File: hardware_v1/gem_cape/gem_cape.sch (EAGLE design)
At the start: 16 parts, among them P8 TSW-123-05-G-D, P9 TSW-123-05-G-D, U1 SN65HVD379, U2 SN65HVD379

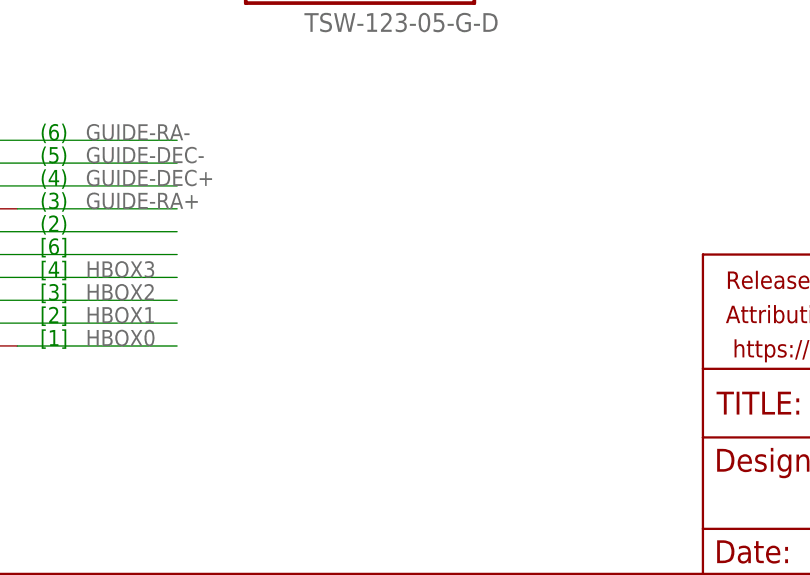
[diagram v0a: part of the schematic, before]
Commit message: hardware_v1/gem_cape: add hpad truth to schematic
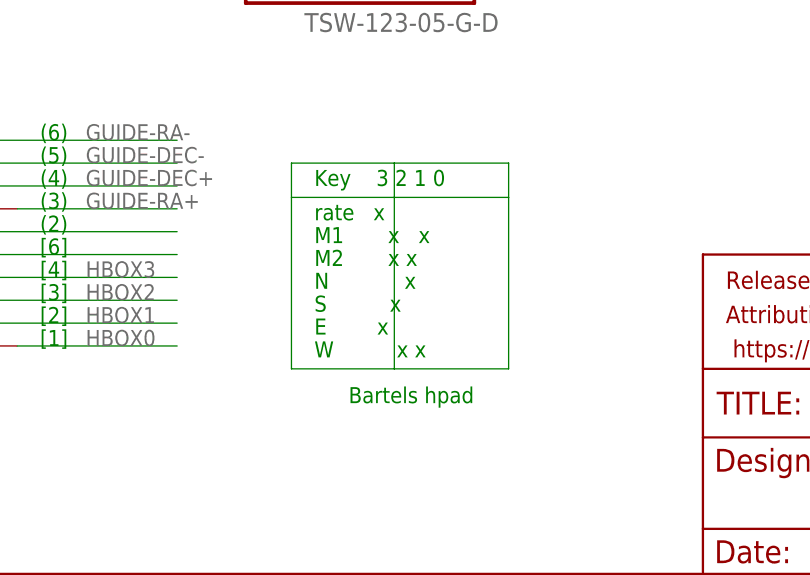
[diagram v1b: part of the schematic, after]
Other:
- note added: "Bartels hpad"
- note added: "E x"
- note added: "Key 3 2 1 0"
- note added: "M1 x x"
- note added: "M2 x x"
- note added: "N x"
- note added: "S x"
- note added: "W x x"
- note added: "rate x"
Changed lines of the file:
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@@
 <setting verticaltext="up"/>
 </settings>
-<grid distance="0.1" unitdist="inch" unit="inch" style="lines" multiple="1" display="no" altdistance="0.01" altunitdist="inch" altunit="inch"/>
+<grid distance="0.05" unitdist="inch" unit="inch" style="lines" multiple="1" display="no" altdistance="0.01" altunitdist="inch" altunit="inch"/>
 <layers>
 <layer number="1" name="Top" color="4" fill="1" visible="no" active="no"/>
@@
 <text x="109.22" y="71.12" size="1.778" layer="91">gpio73</text>
 <text x="101.6" y="68.58" size="1.778" layer="91">gpio70</text>
+<text x="104.14" y="39.37" size="1.778" layer="91" font="fixed">rate   x</text>
+<text x="104.14" y="36.83" size="1.778" layer="91" font="fixed">M1       x   x</text>
+<text x="104.14" y="34.29" size="1.778" layer="91" font="fixed">M2       x x </text>
+<text x="104.14" y="43.18" size="1.778" layer="91" font="fixed">Key    3 2 1 0</text>
+<text x="104.14" y="31.75" size="1.778" layer="91" font="fixed">N            x</text>
+<text x="104.14" y="29.21" size="1.778" layer="91" font="fixed">S          x</text>
+<text x="104.14" y="26.67" size="1.778" layer="91" font="fixed">E        x</text>
+<text x="104.14" y="24.13" size="1.778" layer="91" font="fixed">W          x x</text>
+<text x="107.95" y="19.05" size="1.778" layer="91">Bartels hpad</text>
 </plain>
 <instances>
@@
 </segment>
 </net>
+<net name="N$1" class="0">
+<segment>
+<wire x1="101.6" y1="45.72" x2="113.03" y2="45.72" width="0.1524" layer="91"/>
+<wire x1="113.03" y1="45.72" x2="125.73" y2="45.72" width="0.1524" layer="91"/>
+<wire x1="125.73" y1="45.72" x2="125.73" y2="41.91" width="0.1524" layer="91"/>
+<wire x1="125.73" y1="41.91" x2="125.73" y2="22.86" width="0.1524" layer="91"/>
+<wire x1="125.73" y1="22.86" x2="113.03" y2="22.86" width="0.1524" layer="91"/>
+<wire x1="113.03" y1="22.86" x2="101.6" y2="22.86" width="0.1524" layer="91"/>
+<wire x1="101.6" y1="22.86" x2="101.6" y2="41.91" width="0.1524" layer="91"/>
+<wire x1="101.6" y1="41.91" x2="101.6" y2="45.72" width="0.1524" layer="91"/>
+<wire x1="101.6" y1="41.91" x2="125.73" y2="41.91" width="0.1524" layer="91"/>
+<wire x1="113.03" y1="45.72" x2="113.03" y2="22.86" width="0.1524" layer="91"/>
+</segment>
+</net>

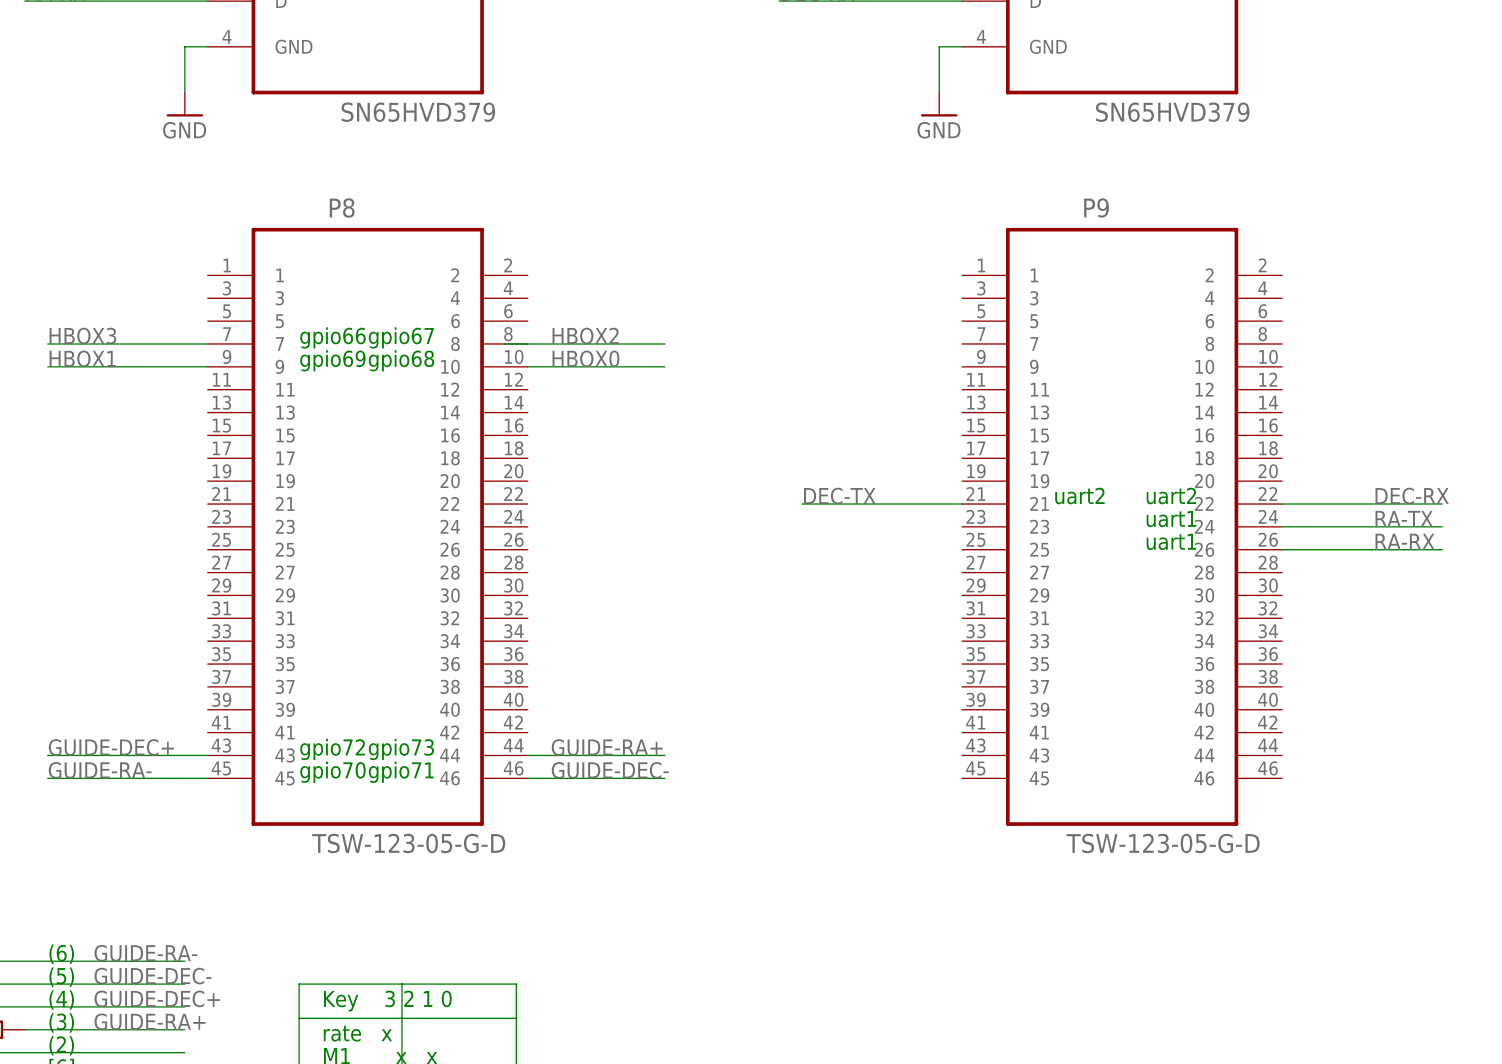
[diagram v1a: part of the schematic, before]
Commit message: hardware_v1/gem_cape: add power pins
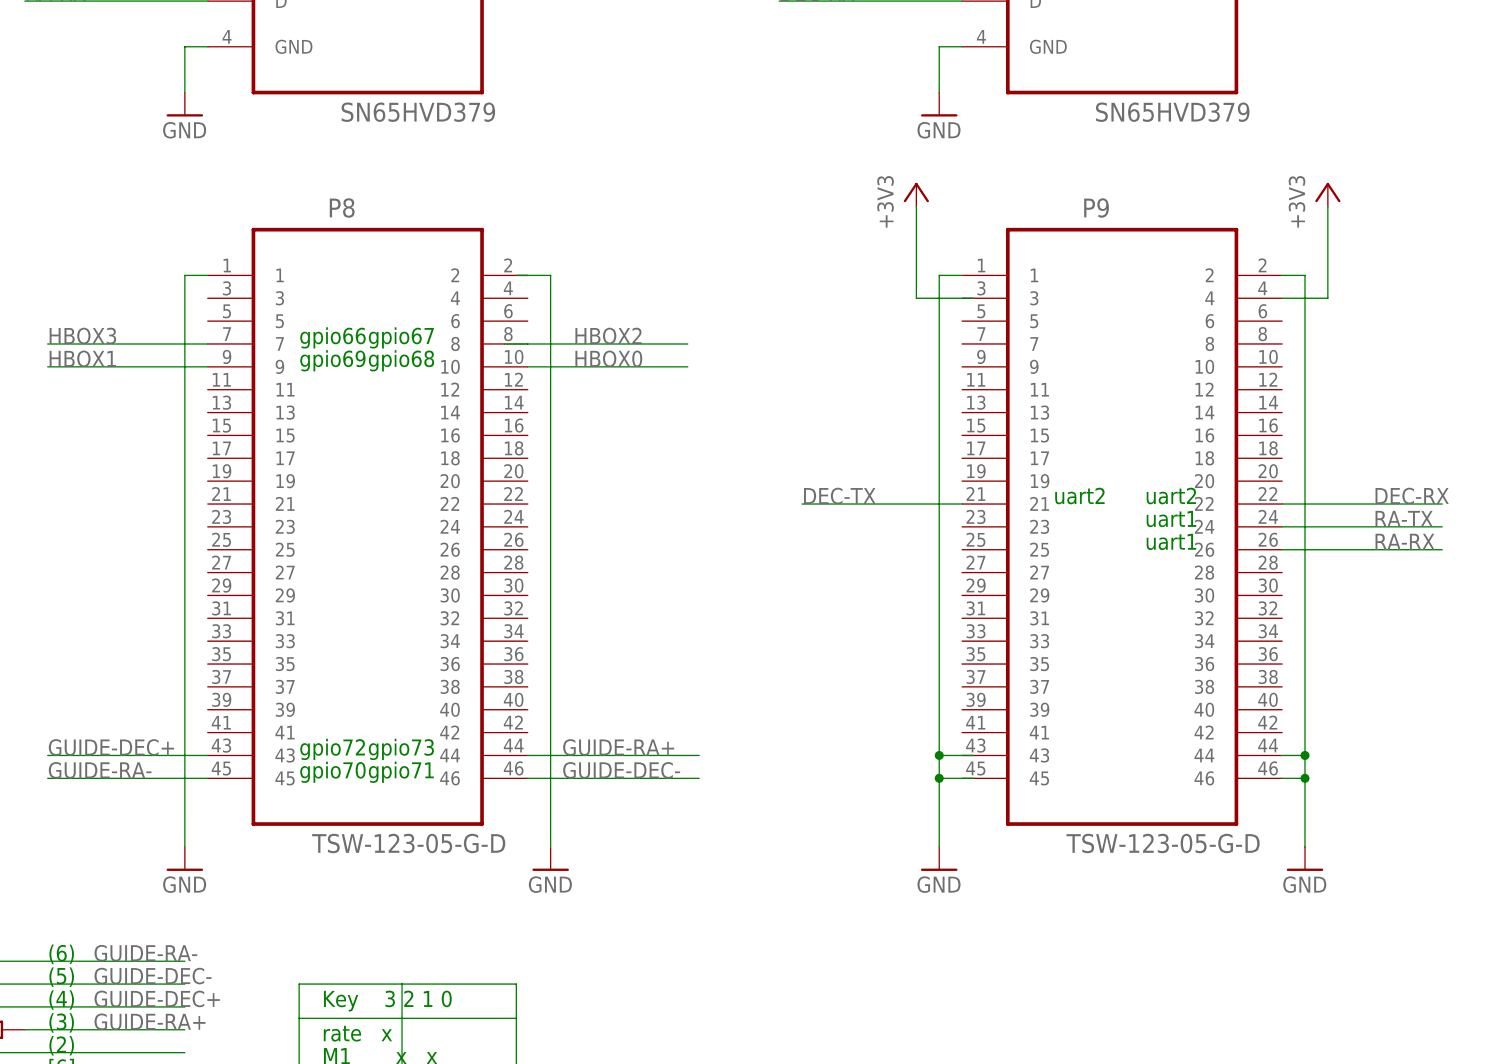
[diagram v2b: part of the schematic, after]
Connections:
- net +3V3: now also P9.4
- net GND: now also P8.1, P9.1, P9.2, P9.44, P9.46
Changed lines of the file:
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@@
 <part name="R7" library="resistor" deviceset="R-EU_" device="R0805" value="220"/>
 <part name="R8" library="resistor" deviceset="R-EU_" device="R0805" value="220"/>
+<part name="GND6" library="supply1" deviceset="GND" device=""/>
+<part name="GND7" library="supply1" deviceset="GND" device=""/>
+<part name="GND8" library="supply1" deviceset="GND" device=""/>
+<part name="GND9" library="supply1" deviceset="GND" device=""/>
+<part name="+3V4" library="supply1" deviceset="+3V3" device=""/>
+<part name="+3V5" library="supply1" deviceset="+3V3" device=""/>
 </parts>
 <sheets>
@@
 <instance part="R7" gate="G$1" x="55.88" y="27.94"/>
 <instance part="R8" gate="G$1" x="66.04" y="25.4"/>
+<instance part="GND6" gate="1" x="88.9" y="58.42"/>
+<instance part="GND7" gate="1" x="129.54" y="58.42"/>
+<instance part="GND8" gate="1" x="172.72" y="58.42"/>
+<instance part="GND9" gate="1" x="213.36" y="58.42"/>
+<instance part="+3V4" gate="G$1" x="215.9" y="134.62"/>
+<instance part="+3V5" gate="G$1" x="170.18" y="134.62"/>
 </instances>
 <busses>
@@
 <junction x="25.4" y="38.1"/>
 </segment>
+<segment>
+<wire x1="176.53" y1="68.58" x2="172.72" y2="68.58" width="0.1524" layer="91"/>
+<wire x1="172.72" y1="68.58" x2="172.72" y2="60.96" width="0.1524" layer="91"/>
+<wire x1="176.53" y1="71.12" x2="172.72" y2="71.12" width="0.1524" layer="91"/>
+<wire x1="172.72" y1="71.12" x2="172.72" y2="68.58" width="0.1524" layer="91"/>
+<junction x="172.72" y="68.58"/>
+<pinref part="P9" gate="A" pin="1"/>
+<wire x1="175.26" y1="124.46" x2="172.72" y2="124.46" width="0.1524" layer="91"/>
+<wire x1="172.72" y1="124.46" x2="172.72" y2="71.12" width="0.1524" layer="91"/>
+<junction x="172.72" y="71.12"/>
+<pinref part="GND8" gate="1" pin="GND"/>
+</segment>
+<segment>
+<pinref part="P9" gate="A" pin="46"/>
+<wire x1="210.82" y1="68.58" x2="213.36" y2="68.58" width="0.1524" layer="91"/>
+<pinref part="P9" gate="A" pin="44"/>
+<wire x1="213.36" y1="68.58" x2="213.36" y2="60.96" width="0.1524" layer="91"/>
+<wire x1="210.82" y1="71.12" x2="213.36" y2="71.12" width="0.1524" layer="91"/>
+<wire x1="213.36" y1="71.12" x2="213.36" y2="68.58" width="0.1524" layer="91"/>
+<junction x="213.36" y="68.58"/>
+<pinref part="P9" gate="A" pin="2"/>
+<wire x1="210.82" y1="124.46" x2="213.36" y2="124.46" width="0.1524" layer="91"/>
+<wire x1="213.36" y1="124.46" x2="213.36" y2="71.12" width="0.1524" layer="91"/>
+<junction x="213.36" y="71.12"/>
+<pinref part="GND9" gate="1" pin="GND"/>
+</segment>
+<segment>
+<wire x1="125.73" y1="124.46" x2="129.54" y2="124.46" width="0.1524" layer="91"/>
+<wire x1="129.54" y1="124.46" x2="129.54" y2="60.96" width="0.1524" layer="91"/>
+<pinref part="GND7" gate="1" pin="GND"/>
+</segment>
+<segment>
+<pinref part="P8" gate="A" pin="1"/>
+<wire x1="91.44" y1="124.46" x2="88.9" y2="124.46" width="0.1524" layer="91"/>
+<wire x1="88.9" y1="124.46" x2="88.9" y2="60.96" width="0.1524" layer="91"/>
+<pinref part="GND6" gate="1" pin="GND"/>
+</segment>
 </net>
 <net name="GUIDE-RA-" class="0">
@@
 <segment>
 <pinref part="P8" gate="A" pin="46"/>
-<wire x1="127" y1="68.58" x2="142.24" y2="68.58" width="0.1524" layer="91"/>
-<label x="129.54" y="68.58" size="1.778" layer="95"/>
+<wire x1="127" y1="68.58" x2="146.05" y2="68.58" width="0.1524" layer="91"/>
+<label x="130.81" y="68.58" size="1.778" layer="95"/>
 </segment>
 <segment>
@@
 <segment>
 <pinref part="P8" gate="A" pin="44"/>
-<wire x1="127" y1="71.12" x2="142.24" y2="71.12" width="0.1524" layer="91"/>
-<label x="129.54" y="71.12" size="1.778" layer="95"/>
+<wire x1="127" y1="71.12" x2="146.05" y2="71.12" width="0.1524" layer="91"/>
+<label x="130.81" y="71.12" size="1.778" layer="95"/>
 </segment>
 <segment>
@@
 <segment>
 <wire x1="124.46" y1="116.84" x2="127" y2="116.84" width="0.1524" layer="91"/>
-<label x="129.54" y="116.84" size="1.778" layer="95"/>
+<label x="132.08" y="116.84" size="1.778" layer="95"/>
 <pinref part="P8" gate="A" pin="8"/>
-<wire x1="127" y1="116.84" x2="142.24" y2="116.84" width="0.1524" layer="91"/>
+<wire x1="127" y1="116.84" x2="144.78" y2="116.84" width="0.1524" layer="91"/>
 </segment>
 <segment>
@@
 <segment>
 <pinref part="P8" gate="A" pin="10"/>
-<wire x1="127" y1="114.3" x2="142.24" y2="114.3" width="0.1524" layer="91"/>
-<label x="129.54" y="114.3" size="1.778" layer="95"/>
+<wire x1="127" y1="114.3" x2="144.78" y2="114.3" width="0.1524" layer="91"/>
+<label x="132.08" y="114.3" size="1.778" layer="95"/>
 </segment>
 <segment>
@@
 <junction x="27.94" y="35.56"/>
 </segment>
-</net>
+<segment>
+<pinref part="P9" gate="A" pin="4"/>
+<pinref part="+3V4" gate="G$1" pin="+3V3"/>
+<wire x1="210.82" y1="121.92" x2="215.9" y2="121.92" width="0.1524" layer="91"/>
+<wire x1="215.9" y1="121.92" x2="215.9" y2="132.08" width="0.1524" layer="91"/>
+</segment>
+<segment>
+<wire x1="176.53" y1="121.92" x2="170.18" y2="121.92" width="0.1524" layer="91"/>
+<wire x1="170.18" y1="121.92" x2="170.18" y2="132.08" width="0.1524" layer="91"/>
+<pinref part="+3V5" gate="G$1" pin="+3V3"/>
+</segment>
+</net>
